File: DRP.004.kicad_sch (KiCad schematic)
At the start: 0 parts

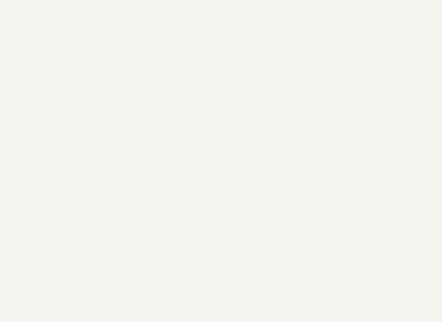
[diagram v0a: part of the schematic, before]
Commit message: v1 Revision - Better routing - Added testpoints - DUCK - Tweaked drawings
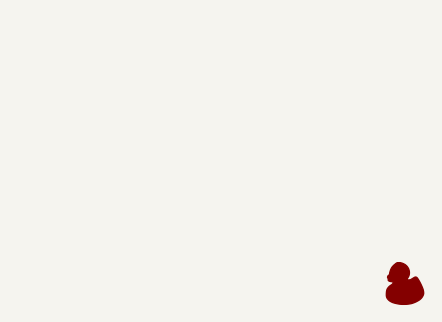
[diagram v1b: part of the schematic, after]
